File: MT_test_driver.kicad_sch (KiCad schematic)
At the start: 64 parts, among them J1 header_SWD, J2 barreljack_5.5mm, J3 16P_USB_C, J4 header_temp, J5 header_mag, SW1 SW_Push, SW2 SW_Push, U1 DRV8871DDA, U2 AMS1117-3.3, U3 INA219AxD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

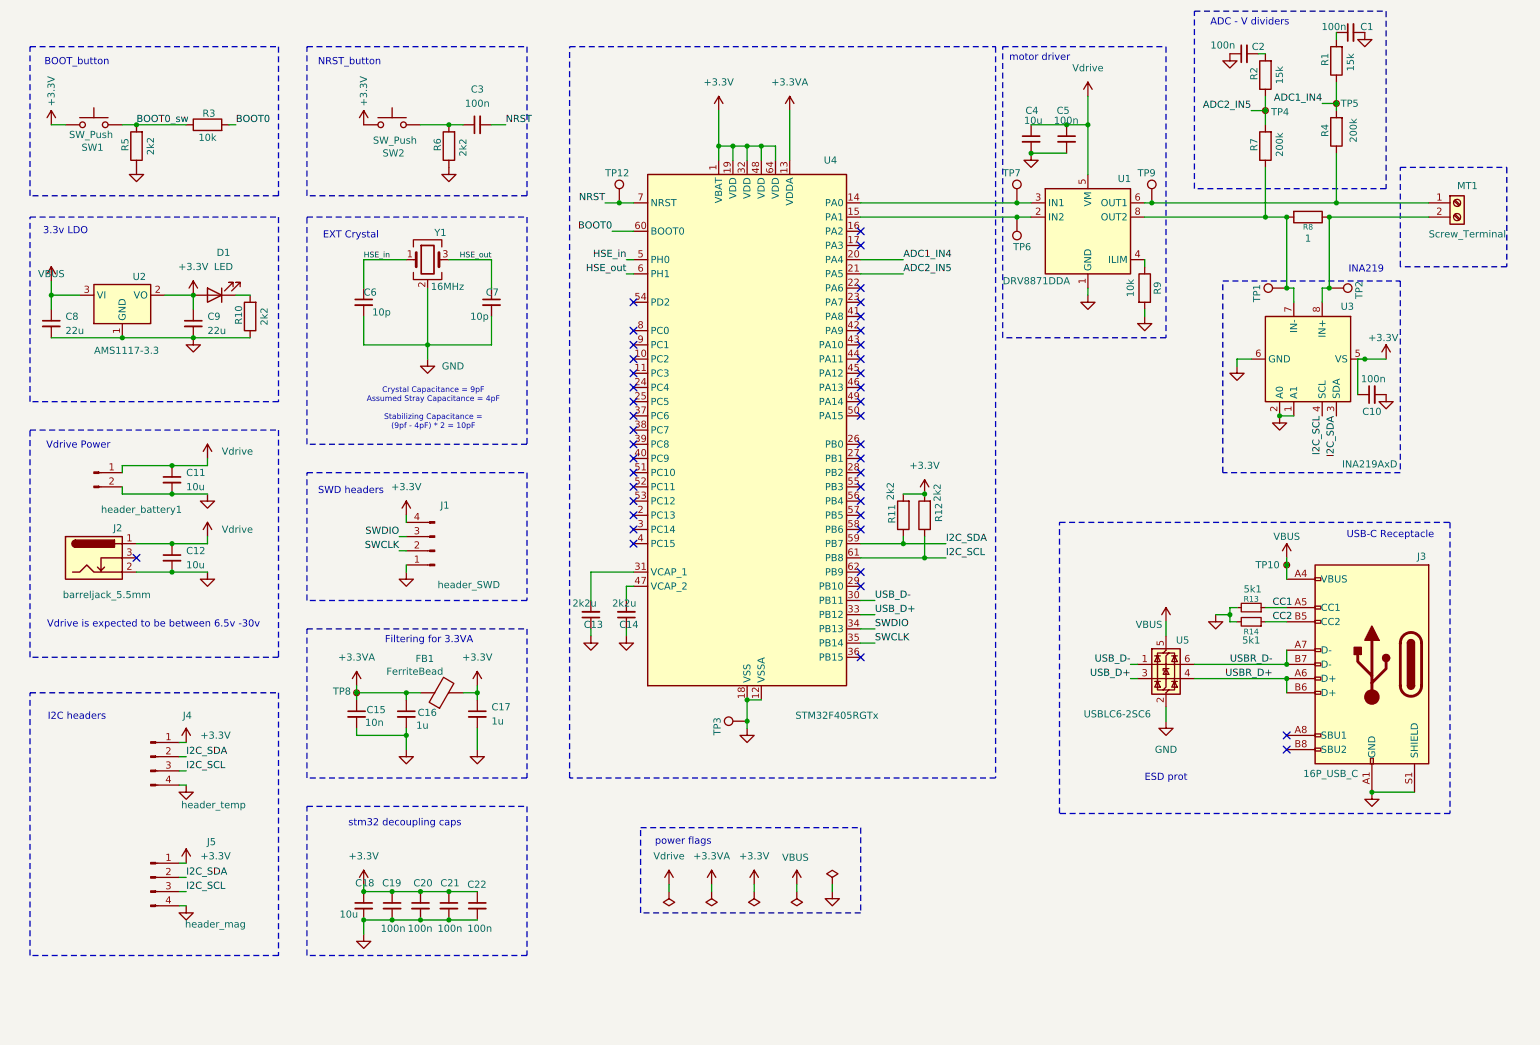
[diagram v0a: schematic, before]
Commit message: pcb layout done, stm32 configuration changed etc
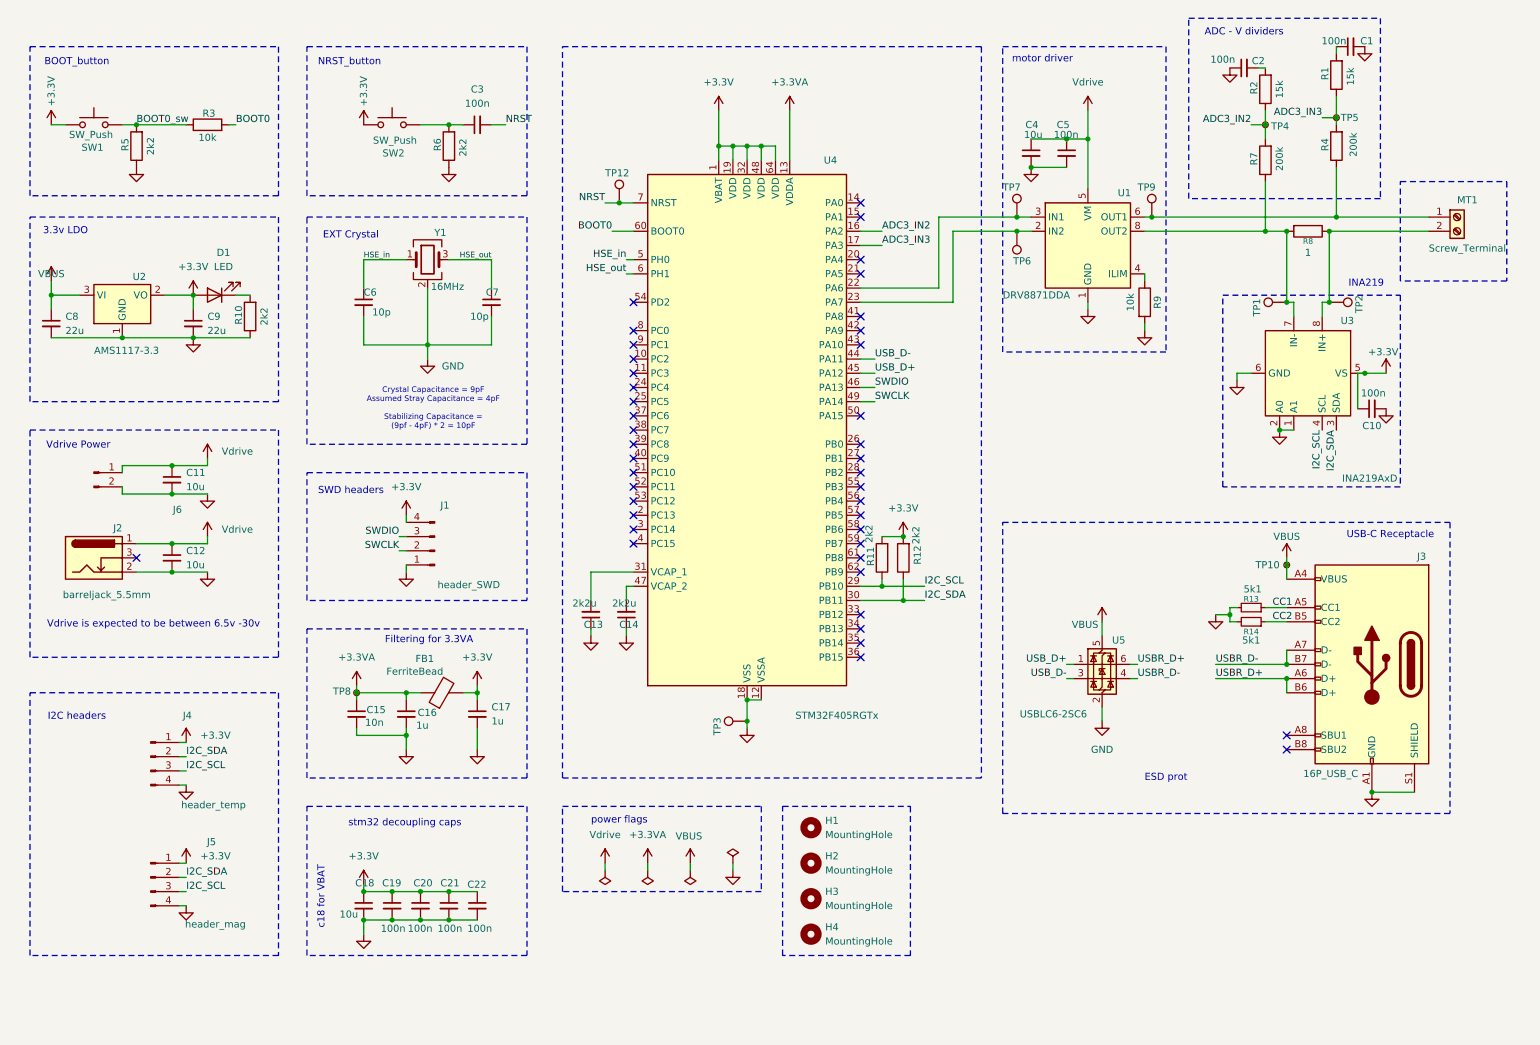
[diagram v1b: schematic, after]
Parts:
- added H1, H2, H3, H4: MountingHole, MountingHole:MountingHole_2.2mm_M2, symbol Mechanical:MountingHole
- J6: renamed from header_battery1; value Conn_01x02_Pin -> header_battery
- MT1: footprint TerminalBlock_Phoenix:TerminalBlock_Phoenix_MPT-0,5-2-2.54_1x02_P2.54mm_Horizontal -> Library:screwterminal_PHOENIX_1751248
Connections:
- net I2C_SCL: now also R11.1, U4.29 (PB10); no longer R12.1, U4.61 (PB8)
- net I2C_SDA: now also R12.1, U4.30 (PB11); no longer R11.1, U4.59 (PB7)
- net SWCLK: now also U4.49 (PA14); no longer U4.35 (PB14)
- net SWDIO: now also U4.46 (PA13); no longer U4.34 (PB13)
- net USBR_D+: now also U5.6 (I/O1); no longer U5.4 (I/O2)
- net USBR_D-: now also U5.4 (I/O2); no longer U5.6 (I/O1)
- net USB_D+: now also U4.45 (PA12), U5.1 (I/O1); no longer U4.33 (PB12), U5.3 (I/O2)
- net USB_D-: now also U4.44 (PA11), U5.3 (I/O2); no longer U4.30 (PB11), U5.1 (I/O1)
- net at TP6.1, U1.2 (IN2): now also U4.23 (PA7); no longer U4.15 (PA1)
- net at TP7.1, U1.3 (IN1): now also U4.22 (PA6); no longer U4.14 (PA0)
- net ADC3_IN2: now reaches U4.16 (PA2)
- net ADC3_IN2: now also R2.1, R7.2, TP4.1
- net ADC3_IN3: now reaches U4.17 (PA3)
- net ADC3_IN3: now also R1.1, R4.2, TP5.1
- removed net ADC1_IN4: R1.1, R4.2, TP5.1, U4.20 (PA4)
- removed net ADC2_IN5: R2.1, R7.2, TP4.1, U4.21 (PA5)
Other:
- note added: "c18 for VBAT"
- moved on the sheet: C1, C10, C2, C4, C5, MT1, R1, R11, R12, R2, R4, R7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

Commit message: Added CAN bus, other small changes
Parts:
- removed H1, H2, H3, H4: MountingHole, MountingHole:MountingHole_2.2mm_M2, symbol Mechanical:MountingHole
- added C23, C24: 100n, Capacitor_SMD:C_0805_2012Metric_Pad1.18x1.45mm_HandSolder, symbol Device:C_Small
- added D2: NUP2105L, Package_TO_SOT_SMD:SOT-23, symbol Power_Protection:NUP2105L
- added H1, H2, H3, H4: MountingHole_Pad, MountingHole:MountingHole_2.2mm_M2_Pad, symbol Mechanical:MountingHole_Pad
- added J7: CAN headers, Connector_PinHeader_2.54mm:PinHeader_1x04_P2.54mm_Vertical, symbol Connector:Conn_01x04_Pin
- added U6: TJA1051T-3, Package_SO:SOIC-8_3.9x4.9mm_P1.27mm, symbol Interface_CAN_LIN:TJA1051T-3
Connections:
- net +3.3V: now also C23.2, U6.5 (VIO)
- net GND: now also C23.1, C24.1, D2.3 (A), H1.1, H2.1, H3.1, H4.1, J7.4 (Pin_4), U6.2 (GND), U6.8 (S)
- net VBUS: now also C24.2, J7.1 (Pin_1), U6.3 (VCC)
- net CAN_RX: now reaches U4.33 (PB12)
- net CAN_RX: now also U6.4 (RXD)
- net CAN_TX: now reaches U4.34 (PB13)
- net CAN_TX: now also U6.1 (TXD)
- new net CAN_H: D2.2 (K), J7.2 (Pin_2), U6.7 (CANH)
- new net CAN_L: D2.1 (K), J7.3 (Pin_3), U6.6 (CANL)
- no-connect marks 42 -> 40
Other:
- note added: "CAN headers"
- moved on the sheet: C11, C12, C15, C16, C17, C18, C19, C20, C21, C22, C6, C7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

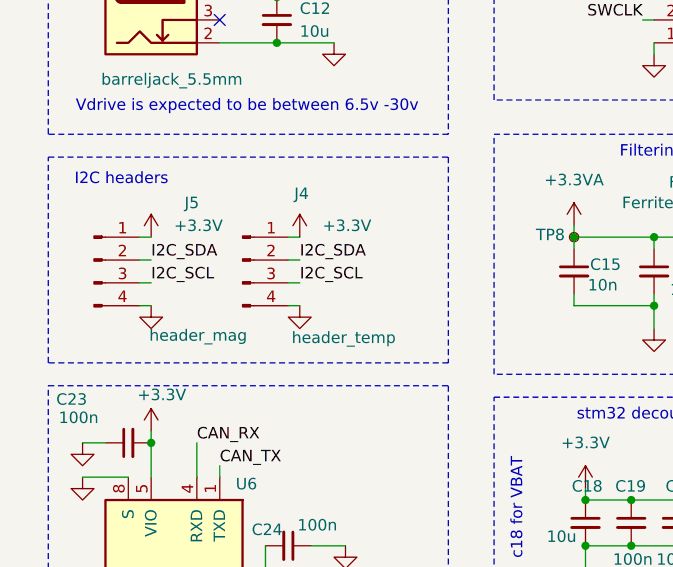
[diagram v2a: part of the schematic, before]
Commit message: changes in layout , moving components
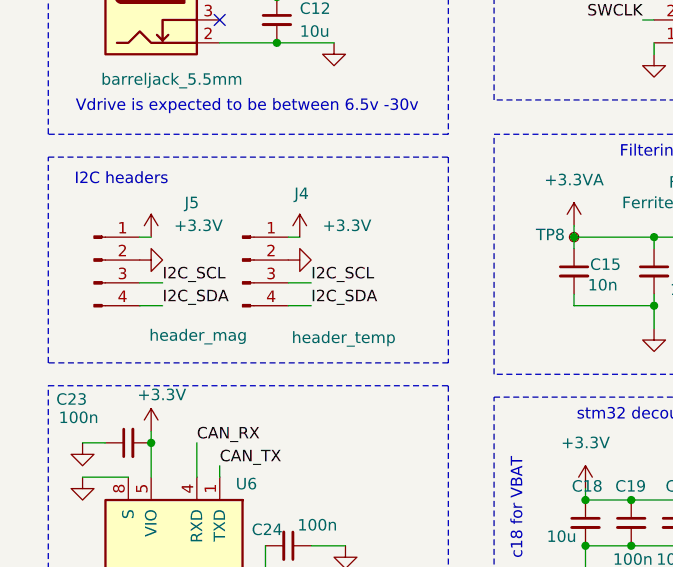
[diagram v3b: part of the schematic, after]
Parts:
- MT1: footprint Library:screwterminal_PHOENIX_1751248 -> TerminalBlock_Phoenix:TerminalBlock_Phoenix_MKDS-1,5-2-5.08_1x02_P5.08mm_Horizontal
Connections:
- net GND: now also J4.2 (Pin_2), J5.2 (Pin_2); no longer J4.4 (Pin_4), J5.4 (Pin_4)
- net I2C_SDA: now also J4.4 (Pin_4), J5.4 (Pin_4); no longer J4.2 (Pin_2), J5.2 (Pin_2)
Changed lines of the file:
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@@
 	(wire
 		(pts
-			(xy 27.94 135.89) (xy 26.67 135.89)
+			(xy 29.21 135.89) (xy 26.67 135.89)
 		)
 		(stroke
@@
 	(wire
 		(pts
-			(xy 27.94 138.43) (xy 26.67 138.43)
-		)
-		(stroke
-			(width 0)
-			(type default)
-		)
-	)
-	(wire
-		(pts
 			(xy 201.93 38.1) (xy 195.58 38.1)
 		)
@@
 	(wire
 		(pts
-			(xy 27.94 133.35) (xy 26.67 133.35)
+			(xy 29.21 138.43) (xy 26.67 138.43)
 		)
 		(stroke
@@
 	(wire
 		(pts
-			(xy 44.45 138.43) (xy 43.18 138.43)
-		)
-		(stroke
-			(width 0)
-			(type default)
-		)
-	)
-	(wire
-		(pts
 			(xy 168.91 116.84) (xy 168.91 118.11)
 		)
@@
 	(wire
 		(pts
-			(xy 44.45 133.35) (xy 43.18 133.35)
+			(xy 45.72 138.43) (xy 43.18 138.43)
 		)
 		(stroke
@@
 	(wire
 		(pts
-			(xy 44.45 135.89) (xy 43.18 135.89)
+			(xy 45.72 135.89) (xy 43.18 135.89)
 		)
 		(stroke
@@
 	)
 	(label "I2C_SDA"
-		(at 44.45 133.35 0)
+		(at 45.72 138.43 0)
 		(effects
 			(font
@@
 	)
 	(label "I2C_SDA"
-		(at 27.94 133.35 0)
+		(at 29.21 138.43 0)
 		(effects
 			(font
@@
 	)
 	(label "I2C_SCL"
-		(at 27.94 135.89 0)
+		(at 29.21 135.89 0)
 		(effects
 			(font
@@
 	)
 	(label "I2C_SCL"
-		(at 44.45 135.89 0)
+		(at 45.72 135.89 0)
 		(effects
 			(font
@@
 			)
 		)
-		(property "Footprint" "Library:screwterminal_PHOENIX_1751248"
+		(property "Footprint" "TerminalBlock_Phoenix:TerminalBlock_Phoenix_MKDS-1,5-2-5.08_1x02_P5.08mm_Horizontal"
 			(at 271.78 52.07 0)
 			(effects
@@
 	(symbol
 		(lib_id "power:GND")
-		(at 44.45 138.43 0)
+		(at 43.18 133.35 90)
 		(unit 1)
 		(exclude_from_sim no)
@@
 		(fields_autoplaced yes)
 		(property "Reference" "#PWR040"
-			(at 44.45 144.78 0)
+			(at 49.53 133.35 0)
 			(effects
 				(font
@@
 		)
 		(property "Value" "GND"
-			(at 44.45 143.51 0)
+			(at 48.26 133.35 0)
 			(effects
 				(font
@@
 		)
 		(property "Footprint" ""
-			(at 44.45 138.43 0)
+			(at 43.18 133.35 0)
 			(effects
 				(font
@@
 		)
 		(property "Datasheet" ""
-			(at 44.45 138.43 0)
+			(at 43.18 133.35 0)
 			(effects
 				(font
@@
 		)
 		(property "Description" "Power symbol creates a global label with name \"GND\" , ground"
-			(at 44.45 138.43 0)
+			(at 43.18 133.35 0)
 			(effects
 				(font
@@
 	(symbol
 		(lib_id "power:GND")
-		(at 27.94 138.43 0)
+		(at 26.67 133.35 90)
 		(unit 1)
 		(exclude_from_sim no)
@@
 		(fields_autoplaced yes)
 		(property "Reference" "#PWR044"
-			(at 27.94 144.78 0)
+			(at 33.02 133.35 0)
 			(effects
 				(font
@@
 		)
 		(property "Value" "GND"
-			(at 27.94 143.51 0)
+			(at 31.75 133.35 0)
 			(effects
 				(font
@@
 		)
 		(property "Footprint" ""
-			(at 27.94 138.43 0)
+			(at 26.67 133.35 0)
 			(effects
 				(font
@@
 		)
 		(property "Datasheet" ""
-			(at 27.94 138.43 0)
+			(at 26.67 133.35 0)
 			(effects
 				(font
@@
 		)
 		(property "Description" "Power symbol creates a global label with name \"GND\" , ground"
-			(at 27.94 138.43 0)
+			(at 26.67 133.35 0)
 			(effects
 				(font

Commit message: final changes
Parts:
- renumbered TP12 to TP11
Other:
- moved on the sheet: TP11
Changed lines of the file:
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@@
 	)
 	(junction
-		(at 121.92 49.53)
-		(diameter 0)
-		(color 0 0 0 0)
-	)
-	(junction
 		(at 81.28 160.02)
 		(diameter 0)
@@
 	)
 	(junction
+		(at 123.19 49.53)
+		(diameter 0)
+		(color 0 0 0 0)
+	)
+	(junction
 		(at 147.32 39.37)
 		(diameter 0)
@@
 	(wire
 		(pts
-			(xy 121.92 49.53) (xy 124.46 49.53)
-		)
-		(stroke
-			(width 0)
-			(type default)
-		)
-	)
-	(wire
-		(pts
 			(xy 33.02 182.88) (xy 33.02 185.42)
 		)
@@
 	(wire
 		(pts
-			(xy 119.38 49.53) (xy 121.92 49.53)
+			(xy 119.38 49.53) (xy 123.19 49.53)
 		)
 		(stroke
@@
 	(wire
 		(pts
+			(xy 123.19 49.53) (xy 124.46 49.53)
+		)
+		(stroke
+			(width 0)
+			(type default)
+		)
+	)
+	(wire
+		(pts
 			(xy 41.91 109.22) (xy 35.56 109.22)
 		)
@@
 	(symbol
 		(lib_id "Connector:TestPoint")
-		(at 121.92 49.53 0)
+		(at 123.19 49.53 0)
 		(unit 1)
 		(exclude_from_sim no)
@@
 		(on_board yes)
 		(dnp no)
-		(property "Reference" "TP12"
-			(at 119.38 44.196 0)
+		(property "Reference" "TP11"
+			(at 120.65 44.196 0)
 			(effects
 				(font
@@
 		)
 		(property "Value" "TestPoint"
-			(at 124.46 47.4979 0)
+			(at 125.73 47.4979 0)
 			(effects
 				(font
@@
 		)
 		(property "Footprint" "TestPoint:TestPoint_Pad_D1.5mm"
-			(at 127 49.53 0)
+			(at 128.27 49.53 0)
 			(effects
 				(font
@@
 		)
 		(property "Datasheet" "~"
-			(at 127 49.53 0)
+			(at 128.27 49.53 0)
 			(effects
 				(font
@@
 		)
 		(property "Description" "test point"
-			(at 121.92 49.53 0)
+			(at 123.19 49.53 0)
 			(effects
 				(font
@@
 			(project "MT_test_driver"
 				(path "/63b7b29e-6d68-4ef7-af6e-6bd9667b85f7"
-					(reference "TP12")
+					(reference "TP11")
 					(unit 1)
 				)

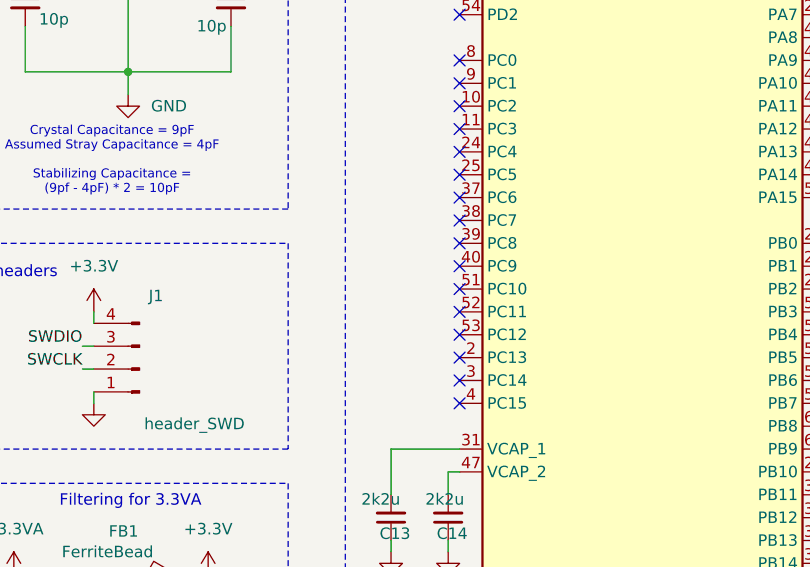
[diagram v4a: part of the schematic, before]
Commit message: added gpio LED for debugging
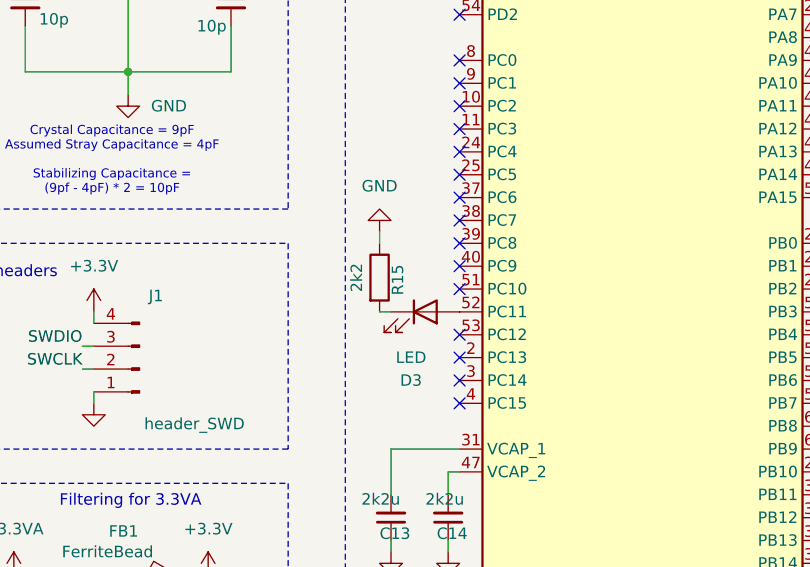
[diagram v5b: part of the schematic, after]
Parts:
- added D3: LED, LED_SMD:LED_0805_2012Metric_Pad1.15x1.40mm_HandSolder, symbol Device:LED
- added R15: 2k2, Resistor_SMD:R_0805_2012Metric_Pad1.20x1.40mm_HandSolder, symbol Device:R
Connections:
- net GND: now also R15.1
- net at U4.52 (PC11): now also D3.2 (A)
- new net: D3.1 (K), R15.2
- no-connect marks 40 -> 39
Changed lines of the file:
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@@
 	)
 	(no_connect
-		(at 124.46 100.33)
-	)
-	(no_connect
 		(at 124.46 107.95)
 	)
@@
 	(wire
 		(pts
+			(xy 115.57 91.44) (xy 115.57 92.71)
+		)
+		(stroke
+			(width 0)
+			(type default)
+		)
+	)
+	(wire
+		(pts
 			(xy 165.1 80.01) (xy 167.64 80.01)
 		)
@@
 	(wire
 		(pts
+			(xy 116.84 100.33) (xy 115.57 100.33)
+		)
+		(stroke
+			(width 0)
+			(type default)
+		)
+	)
+	(wire
+		(pts
 			(xy 58.42 187.96) (xy 57.15 187.96)
 		)
@@
 	)
 	(symbol
+		(lib_id "power:GND")
+		(at 115.57 91.44 180)
+		(unit 1)
+		(exclude_from_sim no)
+		(in_bom yes)
+		(on_board yes)
+		(dnp no)
+		(fields_autoplaced yes)
+		(property "Reference" "#PWR063"
+			(at 115.57 85.09 0)
+			(effects
+				(font
+					(size 1.27 1.27)
+				)
+				(hide yes)
+			)
+		)
+		(property "Value" "GND"
+			(at 115.57 86.36 0)
+			(effects
+				(font
+					(size 1.27 1.27)
+				)
+			)
+		)
+		(property "Footprint" ""
+			(at 115.57 91.44 0)
+			(effects
+				(font
+					(size 1.27 1.27)
+				)
+				(hide yes)
+			)
+		)
+		(property "Datasheet" ""
+			(at 115.57 91.44 0)
+			(effects
+				(font
+					(size 1.27 1.27)
+				)
+				(hide yes)
+			)
+		)
+		(property "Description" "Power symbol creates a global label with name \"GND\" , ground"
+			(at 115.57 91.44 0)
+			(effects
+				(font
+					(size 1.27 1.27)
+				)
+				(hide yes)
+			)
+		)
+		(pin "1"
+		)
+		(instances
+			(project "MT_test_driver"
+				(path "/63b7b29e-6d68-4ef7-af6e-6bd9667b85f7"
+					(reference "#PWR063")
+					(unit 1)
+				)
+			)
+		)
+	)
+	(symbol
 		(lib_id "power:PWR_FLAG")
 		(at 127 168.91 180)
@@
 	)
 	(symbol
+		(lib_id "Device:LED")
+		(at 120.65 100.33 0)
+		(unit 1)
+		(exclude_from_sim no)
+		(in_bom yes)
+		(on_board yes)
+		(dnp no)
+		(fields_autoplaced yes)
+		(property "Reference" "D3"
+			(at 119.0625 107.95 0)
+			(effects
+				(font
+					(size 1.27 1.27)
+				)
+			)
+		)
+		(property "Value" "LED"
+			(at 119.0625 105.41 0)
+			(effects
+				(font
+					(size 1.27 1.27)
+				)
+			)
+		)
+		(property "Footprint" "LED_SMD:LED_0805_2012Metric_Pad1.15x1.40mm_HandSolder"
+			(at 120.65 100.33 0)
+			(effects
+				(font
+					(size 1.27 1.27)
+				)
+				(hide yes)
+			)
+		)
+		(property "Datasheet" "~"
+			(at 120.65 100.33 0)
+			(effects
+				(font
+					(size 1.27 1.27)
+				)
+				(hide yes)
+			)
+		)
+		(property "Description" "Light emitting diode"
+			(at 120.65 100.33 0)
+			(effects
+				(font
+					(size 1.27 1.27)
+				)
+				(hide yes)
+			)
+		)
+		(property "Sim.Pins" "1=K 2=A"
+			(at 120.65 100.33 0)
+			(effects
+				(font
+					(size 1.27 1.27)
+				)
+				(hide yes)
+			)
+		)
+		(pin "2"
+		)
+		(pin "1"
+		)
+		(instances
+			(project "MT_test_driver"
+				(path "/63b7b29e-6d68-4ef7-af6e-6bd9667b85f7"
+					(reference "D3")
+					(unit 1)
+				)
+			)
+		)
+	)
+	(symbol
 		(lib_id "power:GND")
 		(at 20.32 157.48 0)
@@
 					(unit 1)
 				)
+			)
+		)
+	)
+	(symbol
+		(lib_id "Device:R")
+		(at 115.57 96.52 0)
+		(unit 1)
+		(exclude_from_sim no)
+		(in_bom yes)
+		(on_board yes)
+		(dnp no)
+		(property "Reference" "R15"
+			(at 117.602 96.774 90)
+			(effects
+				(font
+					(size 1.27 1.27)
+				)
+			)
+		)
+		(property "Value" "2k2"
+			(at 113.03 96.52 90)
+			(effects
+				(font
+					(size 1.27 1.27)
+				)
+			)
+		)
+		(property "Footprint" "Resistor_SMD:R_0805_2012Metric_Pad1.20x1.40mm_HandSolder"
+			(at 113.792 96.52 90)
+			(effects
+				(font
+					(size 1.27 1.27)
+				)
+				(hide yes)
+			)
+		)
+		(property "Datasheet" "~"
+			(at 115.57 96.52 0)
+			(effects
+				(font
+					(size 1.27 1.27)
+				)
+				(hide yes)
+			)
+		)
+		(property "Description" "Resistor"
+			(at 115.57 96.52 0)
+			(effects
+				(font
+					(size 1.27 1.27)
+				)
+				(hide yes)
+			)
+		)
+		(pin "1"
+		)
+		(pin "2"
+		)
+		(instances
+			(project "MT_test_driver"
+				(path "/63b7b29e-6d68-4ef7-af6e-6bd9667b85f7"
+					(reference "R15")
+					(unit 1)
+				)
